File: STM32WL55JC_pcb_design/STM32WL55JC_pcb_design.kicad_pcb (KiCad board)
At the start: 4 copper layers, 131 parts, among them IC1 STM32F051R8T6, IC2 CY8C9540A-24PVXIT, IC3 SX1276IMLTRT, IC4 PE4259, IC5 PE4259, IC6 HTS221TR, J1 Conn_01x03, J10 Conn_02x15_Odd_Even, J11 Conn_02x02_Odd_Even, J12 Conn_01x10, J13 Conn_01x10, J14 Conn_01x10, J15 Conn_01x10, J16 Conn_Coaxial, J17 Conn_Coaxial, J18 CT3151-2, J19 CT3151-2, J2 Conn_01x03, J20 USB_A, J21 Conn_02x02_Odd_Even, J3 Conn_01x03, J4 Conn_01x09, J5 Conn_01x09, J6 Conn_01x03, J7 Conn_01x09, J8 Conn_01x09, J9 Conn_02x10_Odd_Even, Q1 AO3401A, SW1 SW_MEC_5E, SW2 SW_MEC_5E, U1 DS1307+, U2 L80-M39, U3 LIS3DHTR, U4 AMS1117-3.3, U5 AMS1117-5.0, Y1 32MHz, Y2 32.768kHz, Y3 32MHz, Y4 32.768kHz

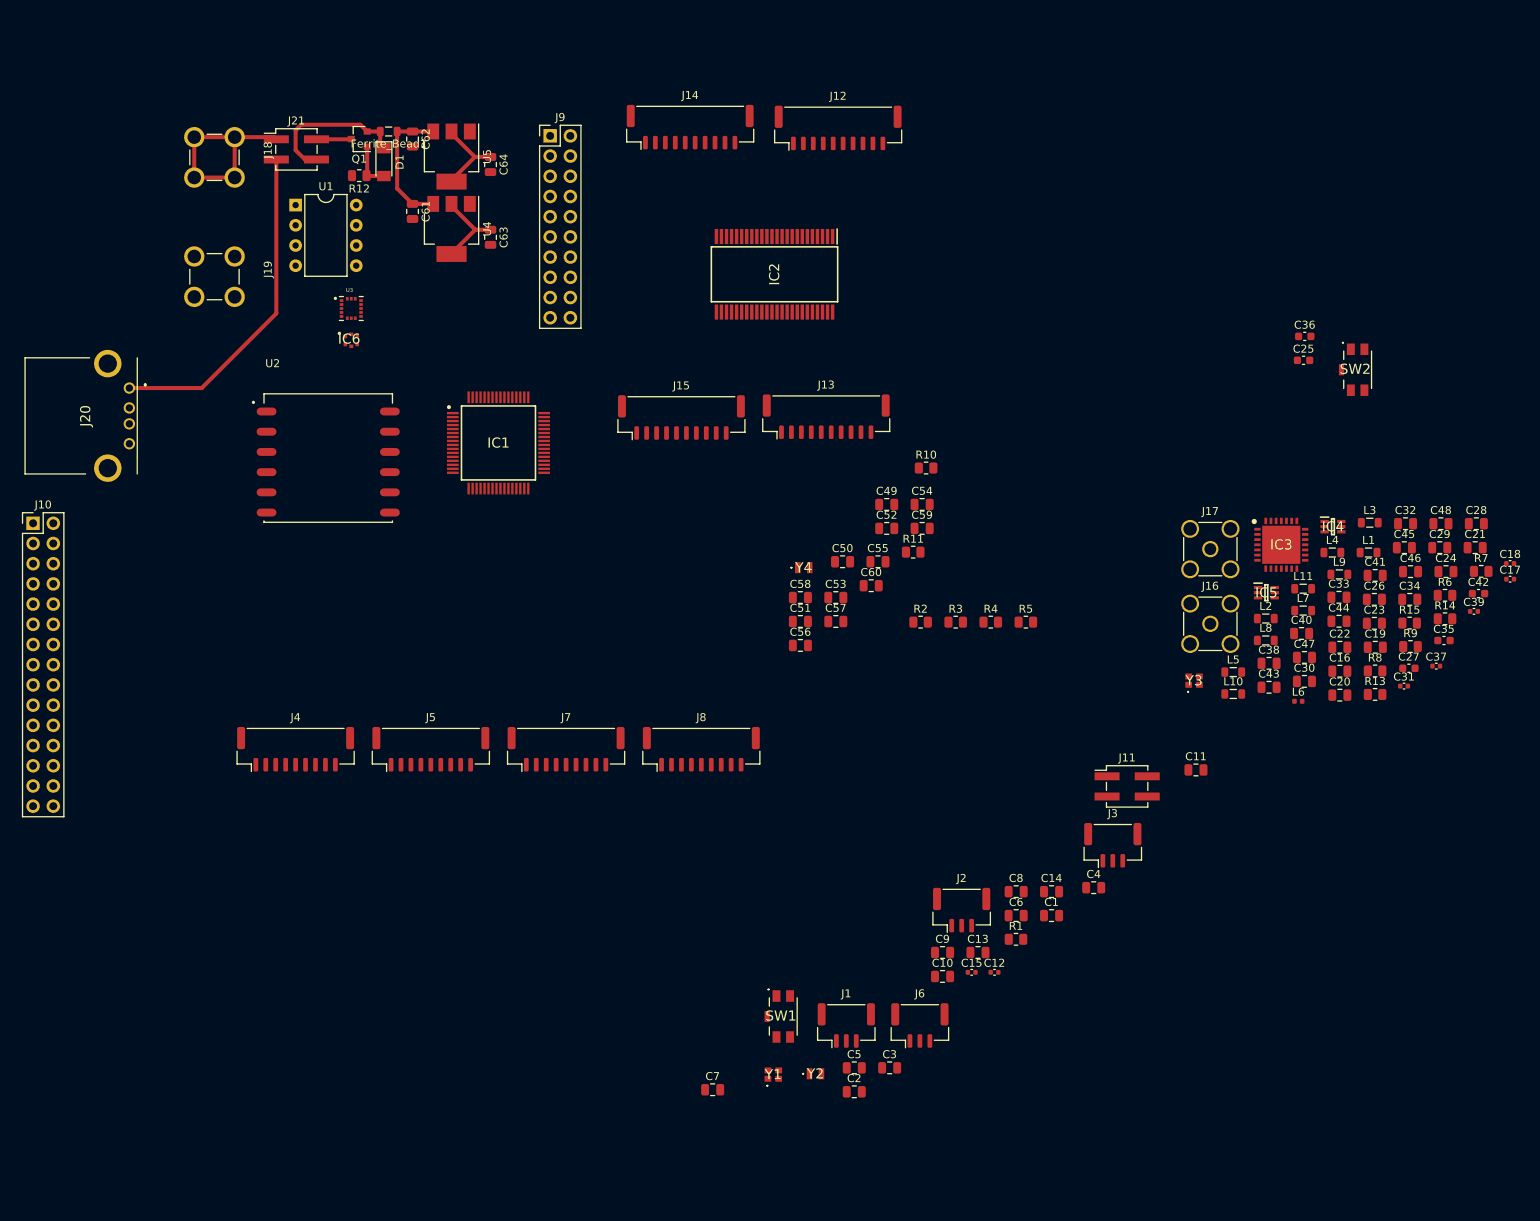
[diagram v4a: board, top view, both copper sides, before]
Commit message: Initial pcb layout and routing
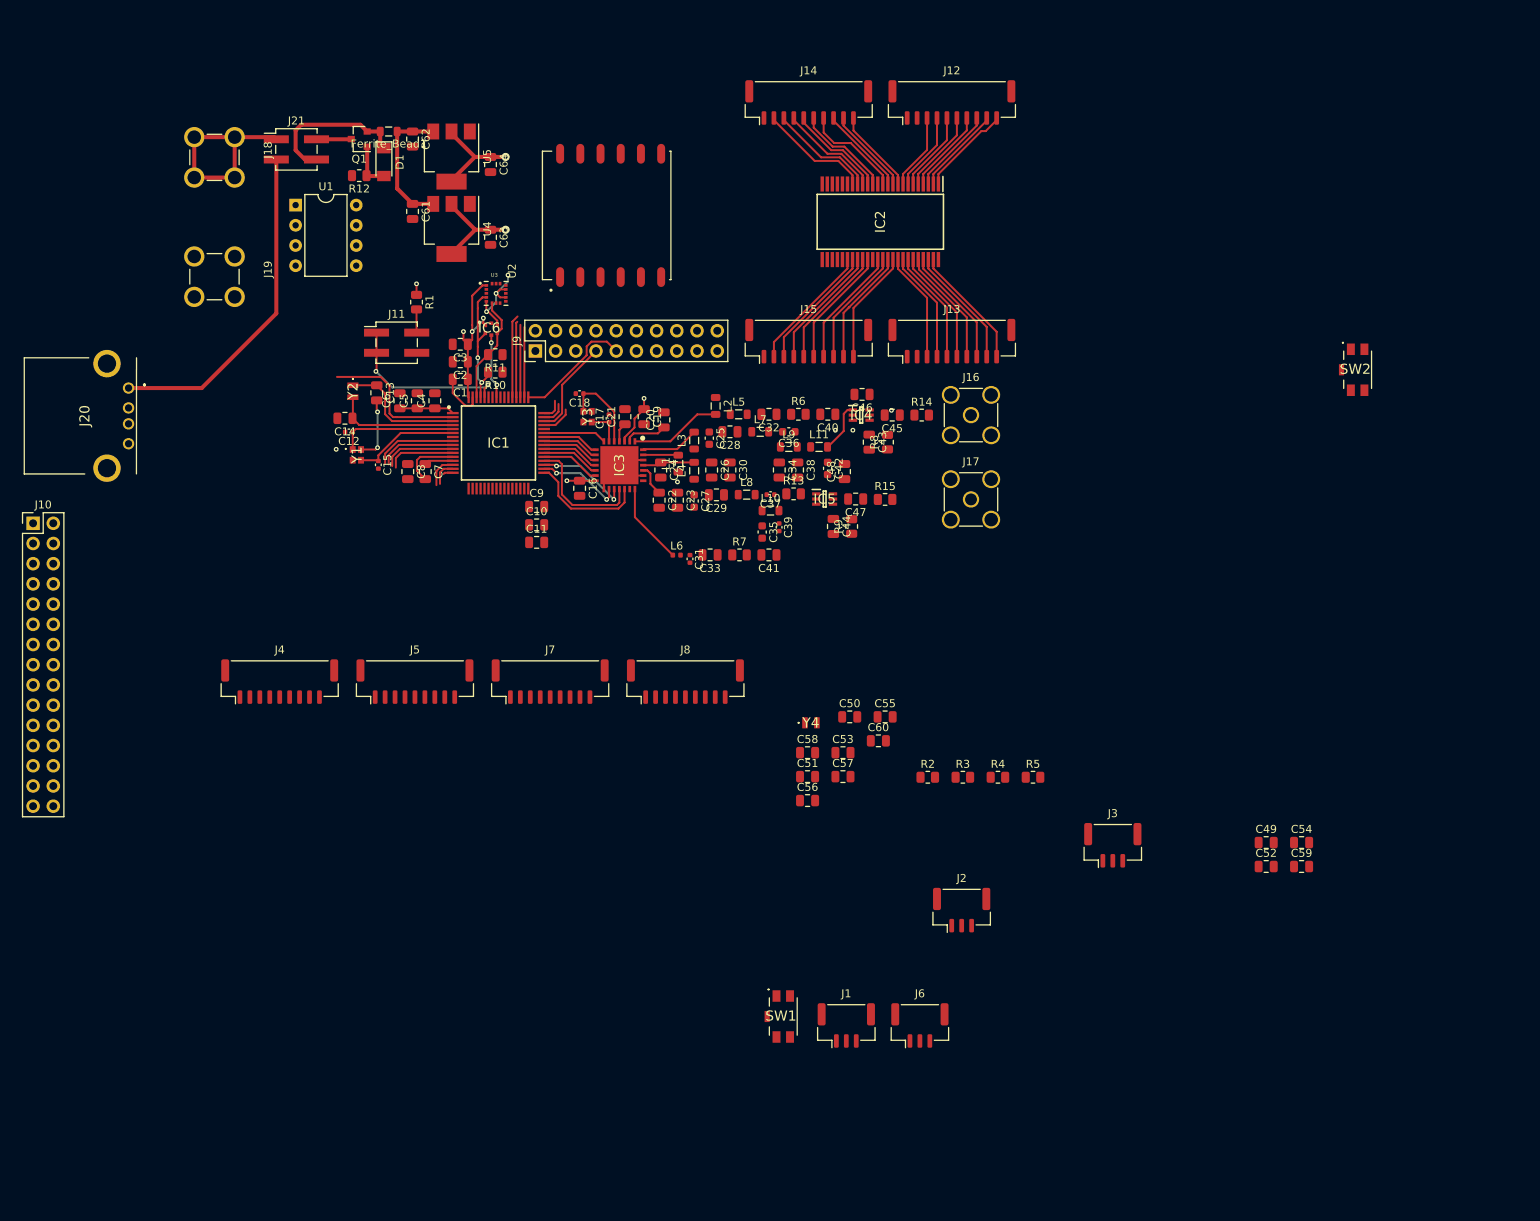
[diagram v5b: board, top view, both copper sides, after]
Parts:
- J20: value USB_A -> USB-A-S-F-B-TH
- moved C18 118.9 mm to (149.7, 79.7), turned to 180 degrees
- moved C17 115.1 mm to (153.4, 82.8), turned to 90 degrees
- moved R1 110.0 mm to (129.2, 68.2), turned to 270 degrees
- moved C21 108.1 mm to (155.4, 82.6), turned to 90 degrees
- moved J11 107.4 mm to (126.7, 73.3)
- moved C14 106.9 mm to (120.2, 82.8), turned to 180 degrees
- moved C12 105.8 mm to (120.7, 84.5), turned to 180 degrees
- moved C3 105.8 mm to (134.7, 73.5), turned to 180 degrees
- moved C2 104.3 mm to (134.7, 75.7), turned to 180 degrees
- moved Y2 103.6 mm to (121.2, 79.4), turned to 270 degrees
- moved C13 103.3 mm to (124.2, 79.6), turned to 270 degrees
- moved C4 103.0 mm to (131.5, 80.6), turned to 90 degrees
- moved C6 100.9 mm to (127.1, 80.6), turned to 90 degrees
- moved C1 100.3 mm to (134.7, 77.9), turned to 180 degrees
- moved C5 100.2 mm to (129.3, 80.6), turned to 90 degrees
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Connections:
- J20 pad MH1: (no net) -> Net-(J20-PadMH1)
- J20 pad MH2: (no net) -> Net-(J20-PadMH2)
- SW1 pad 1: Net-(SW1-Pad1) -> NRST
- SW1 pad 2: Net-(SW1-Pad2) -> GNDREF
- SW1 pad 3: Net-(SW1-Pad3) -> NRST
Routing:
- net VDD: track 10.7 -> 59.0 mm, vias 0 -> 9
- net GNDREF: track 0.00 -> 44.4 mm, vias 0 -> 6
- net BOOT0: track 0.00 -> 21.6 mm, vias 0 -> 2
- net PC13: track 0.00 -> 18.7 mm
- net SCL: track 0.00 -> 16.6 mm, vias 0 -> 2
- net ENC_RST_4: track 0.00 -> 16.0 mm
- net OSC32_IN: track 0.00 -> 15.9 mm
- net LoRa_MOSI: track 0.00 -> 15.8 mm
- net ENC8_4: track 0.00 -> 15.8 mm
- net OSC32_OUT: track 0.00 -> 15.6 mm
- net ENC8_3: track 0.00 -> 15.5 mm
- net ENC5_1: track 0.00 -> 15.5 mm
- net ENC8_2: track 0.00 -> 15.3 mm
- net ENC5_2: track 0.00 -> 15.2 mm
- net SWCLK: track 0.00 -> 15.1 mm
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
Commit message: Finish pcb routing
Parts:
- removed C50, C52: 15pF, Capacitor_SMD:C_0805_2012Metric
- removed C51, C54, C59: 10uF, Capacitor_SMD:C_0805_2012Metric
- removed C53, C58, C60: 100nF, Capacitor_SMD:C_0805_2012Metric
- removed U1: DS1307+, Package_DIP:DIP-8_W7.62mm
- removed Y4: 32.768kHz, SC20S-12.5PF20PPM:SC20S125PF20PPM
- added J22: Conn_01x20_Male, Connector_PinHeader_2.54mm:PinHeader_1x20_P2.54mm_Vertical, F.Cu at (119.3, 41.2)
- J10: value Conn_02x15_Odd_Even -> Conn_01x08_Male; footprint Connector_PinHeader_2.54mm:PinHeader_2x15_P2.54mm_Vertical -> Connector_PinHeader_2.54mm:PinHeader_1x08_P2.54mm_Vertical
- moved J3 122.9 mm to (102.2, 92.0)
- moved J1 110.2 mm to (102.2, 84.4)
- moved J2 105.3 mm to (111.4, 84.4)
- moved J6 105.3 mm to (111.4, 92.0)
- moved SW1 103.7 mm to (115.9, 73.0), turned to 90 degrees
- moved C49 82.0 mm to (197.9, 63.5)
- moved R3 81.5 mm to (174.9, 49.7), turned to 270 degrees
- moved R2 81.0 mm to (172.4, 49.7), turned to 270 degrees
- moved R4 77.9 mm to (177.8, 54.0), turned to 90 degrees
- moved R5 77.0 mm to (200.4, 51.2), turned to 270 degrees
- moved J10 70.3 mm to (148.2, 116.6), turned to 270 degrees
- moved C57 66.2 mm to (167.8, 63.4), turned to 270 degrees
- moved C56 65.0 mm to (165.5, 67.1), turned to 270 degrees
- moved C55 61.3 mm to (165.5, 63.4), turned to 270 degrees
- moved SW2 51.5 mm to (199.6, 57.8)
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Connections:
- C49 pad 1: 5V -> VDD
- IC1 pad 10: ADC_CNVST1_2 -> ADC_CS1_2
- IC1 pad 11: ADC_CNVST2_1 -> ADC_CNVST1_1
- IC1 pad 14: ADC_CNVST2_2 -> ADC_CS1_1
- IC1 pad 15: ADC_CNVST3_1 -> ADC_CNVST2_2
- IC1 pad 16: ADC_CNVST3_2 -> ADC_CS2_2
- IC1 pad 17: ADC_CS1_1 -> ADC_CNVST2_1
- IC1 pad 18: ADC_CS1_2 -> ADC_CS2_1
- IC1 pad 19: ADC_CS2_1 -> ADC_CNVST3_2
- IC1 pad 20: ADC_CS2_2 -> ADC_CS3_2
- IC1 pad 24: ADC_CS3_1 -> ADC_CNVST3_1
- IC1 pad 25: ADC_CS3_2 -> ADC_CS3_1
- IC1 pad 26: ADC_CS4_1 -> ADC_CNVST4_2
- IC1 pad 29: ADC_CNVST4_2 -> ADC_CS4_1
- IC1 pad 50: OR1 -> OR3
- IC1 pad 51: OR2 -> OR4
- IC1 pad 52: OR3 -> OR2
- IC1 pad 53: OR4 -> OR1
- IC1 pad 9: ADC_CNVST1_1 -> ADC_CNVST1_2
- J10 pad 1: PA11 -> ADC_EOC4_1
- J10 pad 2: ACC_ADC1 -> ADC_EOC4_2
- J10 pad 3: PB3 -> ADC_EOC3_1
- J10 pad 4: ACC_ADC2 -> ADC_EOC3_2
- J10 pad 5: PB4 -> ADC_EOC2_1
- J10 pad 6: ACC_ADC3 -> ADC_EOC2_2
- J10 pad 7: PC0 -> ADC_EOC1_1
- J10 pad 8: ACC_INT1 -> ADC_EOC1_2
- J9 pad 13: Net-(J9-Pad13) -> GNDREF
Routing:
- net VDD: track 59.0 -> 572.9 mm, vias 9 -> 26
- net GNDREF: track 44.4 -> 252.5 mm, vias 6 -> 32
- net ADC_DOUT: track 0.00 -> 86.5 mm, vias 0 -> 6
- net 5V: track 12.6 -> 98.6 mm, vias 1 -> 3
- net ADC_DIN: track 0.00 -> 84.3 mm, vias 0 -> 4
- net ADC_SCLK: track 0.00 -> 82.7 mm
- net LoRa_RXTX_CTRL: track 0.00 -> 77.1 mm, vias 0 -> 2
- net OR1: track 8.81 -> 82.6 mm
- net ADC_EOC3_2: track 0.00 -> 63.2 mm, vias 0 -> 1
- net EXP_SCL: track 3.07 -> 63.2 mm, vias 0 -> 2
- net NRST: track 0.00 -> 58.7 mm, vias 0 -> 3
- net ADC_EOC2_1: track 0.00 -> 53.4 mm, vias 0 -> 1
- net EXP_SDA: track 2.71 -> 55.6 mm, vias 0 -> 2
- net PB3: track 0.00 -> 52.9 mm, vias 0 -> 1
- net OR2: track 9.11 -> 61.9 mm
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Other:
- copper layers 4 -> 2

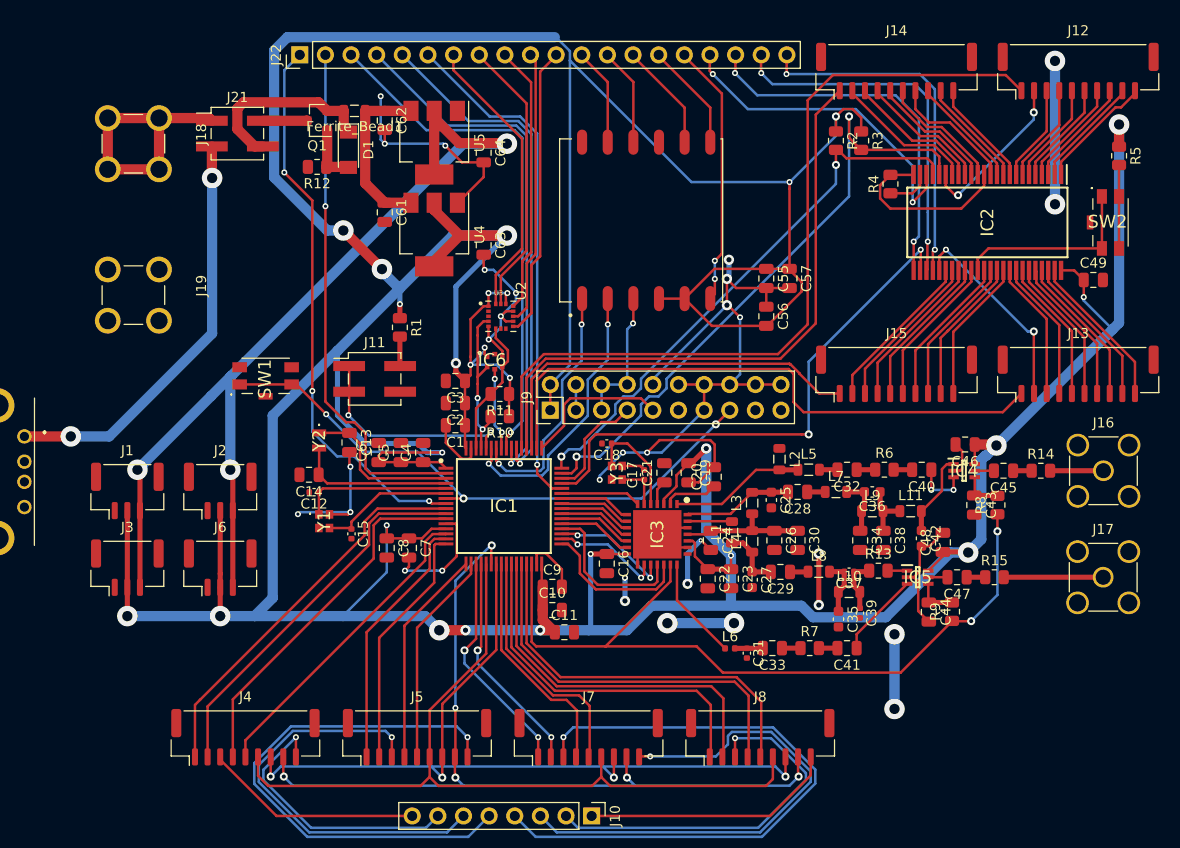
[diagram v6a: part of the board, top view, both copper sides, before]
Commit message: Remove acid traps, make vias the same size, and improve wire spacing
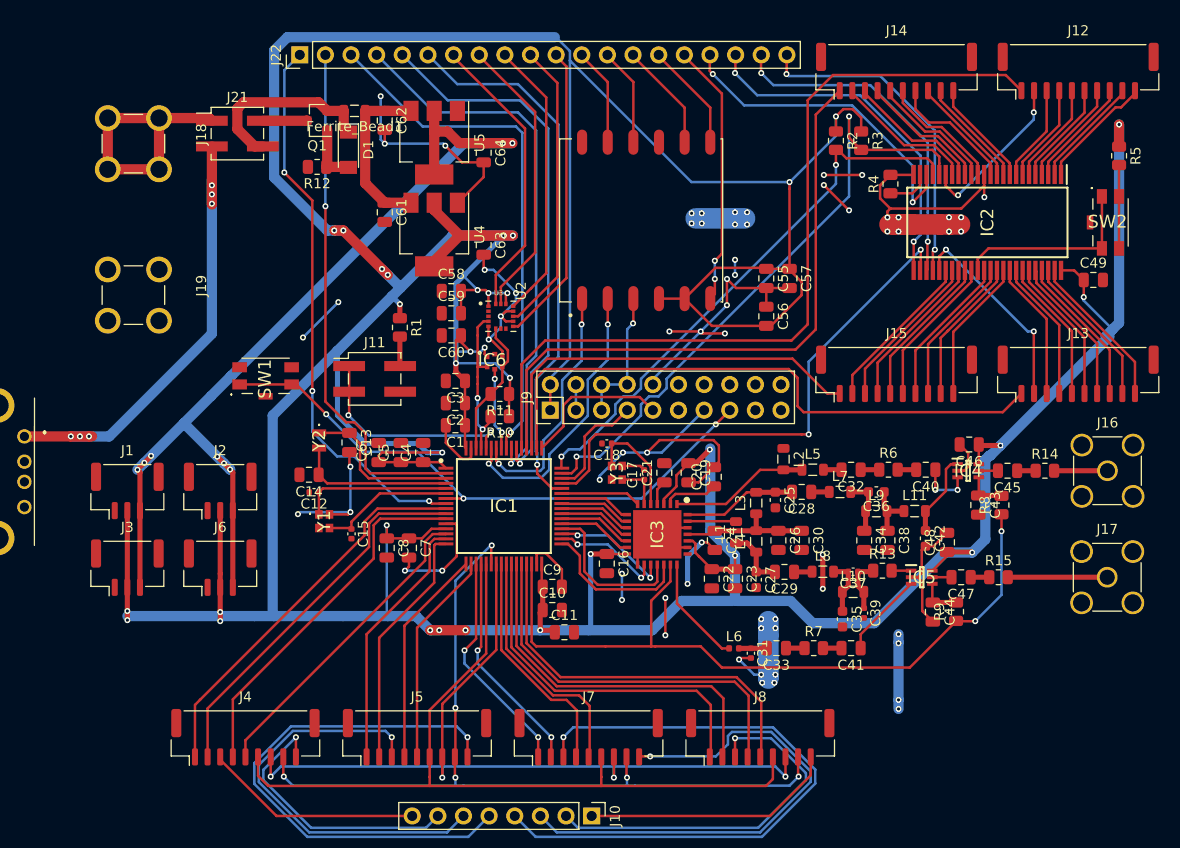
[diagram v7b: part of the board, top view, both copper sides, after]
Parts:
- added C58: 100nF, Capacitor_SMD:C_0805_2012Metric, F.Cu at (134.3, 64.6)
- added C59: 10uF, Capacitor_SMD:C_0805_2012Metric, F.Cu at (134.3, 66.8)
- added C60: 100nF, Capacitor_SMD:C_0805_2012Metric, F.Cu at (134.3, 69.0)
- moved C22 0.40 mm to (160.1, 93.1)
- moved C23 0.40 mm to (162.4, 93.1)
- moved C24 0.40 mm to (160.4, 89.3)
- moved C25 0.40 mm to (166.4, 85.3)
- moved C27 0.40 mm to (164.5, 93.2)
- moved C28 0.40 mm to (169.0, 84.5)
- moved C29 0.40 mm to (167.3, 92.4)
- moved C30 0.40 mm to (169.0, 89.3)
- moved C31 0.40 mm to (164.0, 100.5)
- moved C32 0.40 mm to (173.9, 82.3)
- moved C33 0.40 mm to (166.5, 100.0)
- moved C35 0.40 mm to (173.1, 97.1)
- moved C36 0.40 mm to (176.4, 84.5)
- moved C37 0.40 mm to (174.1, 92.4)
- moved C38 0.40 mm to (177.5, 89.3)
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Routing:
- net VDD: track 572.9 -> 580.9 mm, vias 26 -> 33
- net +5V: track 41.4 -> 45.9 mm, vias 2 -> 6
- net PA11: track 50.8 -> 54.4 mm
- net PD2: track 50.8 -> 53.5 mm
- net EXP_1: track 36.4 -> 33.8 mm
- net EXP_0: track 35.2 -> 32.8 mm
- net GNDREF: track 252.5 -> 254.8 mm, vias 32 -> 67
- net EXP_2: track 37.1 -> 35.2 mm
- net LoRa_RXTX_CTRL: track 77.1 -> 75.2 mm
- net ACC_INT1: track 27.2 -> 29.0 mm
- net PB3: track 52.9 -> 54.5 mm
- net 5V: track 98.6 -> 100.2 mm, vias 3 -> 8
- net ACC_ADC3: track 26.6 -> 27.9 mm
- net ADC_DIN: track 84.3 -> 83.4 mm
- net ACC_INT2: track 28.8 -> 29.7 mm
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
